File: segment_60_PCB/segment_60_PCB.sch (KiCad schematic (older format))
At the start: 118 parts, among them J1 BREAKOUT, SW1 SW_Push_45deg, SW10 SW_Push_45deg, SW11 SW_Push_45deg, SW12 SW_Push_45deg, SW13 SW_Push_45deg, SW14 SW_Push_45deg, SW15 SW_Push_45deg, SW16 SW_Push_45deg, SW17 SW_Push_45deg, SW18 SW_Push_45deg, SW19 SW_Push_45deg, SW2 SW_Push_45deg, SW20 SW_Push_45deg, SW21 SW_Push_45deg, SW22 SW_Push_45deg, SW23 SW_Push_45deg, SW24 SW_Push_45deg, SW25 SW_Push_45deg, SW26 SW_Push_45deg, SW27 SW_Push_45deg, SW28 SW_Push_45deg, SW29 SW_Push_45deg, SW3 SW_Push_45deg, SW30 SW_Push_45deg, SW31 SW_Push_45deg, SW32 SW_Push_45deg, SW33 SW_Push_45deg, SW34 SW_Push_45deg, SW35 SW_Push_45deg, SW36 SW_Push_45deg, SW37 SW_Push_45deg, SW38 SW_Push_45deg, SW39 SW_Push_45deg, SW4 SW_Push_45deg, SW40 SW_Push_45deg, SW41 SW_Push_45deg, SW42 SW_Push_45deg, SW43 SW_Push_45deg, SW44 SW_Push_45deg, SW45 SW_Push_45deg, SW46 SW_Push_45deg, SW47 SW_Push_45deg, SW48 SW_Push_45deg, SW49 SW_Push_45deg, SW5 SW_Push_45deg, SW50 SW_Push_45deg, SW51 SW_Push_45deg, SW52 SW_Push_45deg, SW53 SW_Push_45deg, SW54 SW_Push_45deg, SW55 SW_Push_45deg, SW56 SW_Push_45deg, SW57 SW_Push_45deg, SW58 SW_Push_45deg, SW59 SW_Push_45deg, SW6 SW_Push_45deg, SW60 SW_Push_45deg, SW61 SW_Push_45deg, SW62 SW_Push_45deg, SW63 SW_Push_45deg, SW64 SW_Push_45deg, SW65 SW_Push_45deg, SW66 SW_Push, SW67 SW_Push, SW7 SW_Push_45deg, SW8 SW_Push_45deg, SW9 SW_Push_45deg, U1 ATmega328P-PU, U10 74HC365, U11 74HC365, U12 74HC365, U13 74HC365, U14 74HC365, U15 74HC365, U16 74HC365, U17 74HC365, U2 74HC138, U3 74HC138, U4 74HC365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

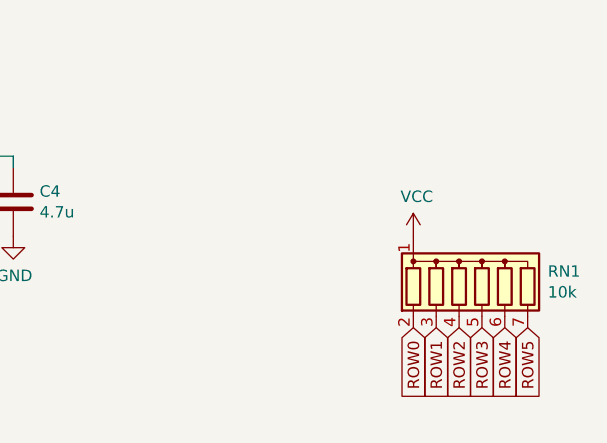
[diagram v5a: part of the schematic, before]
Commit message: added border, changed J1 footprint and model
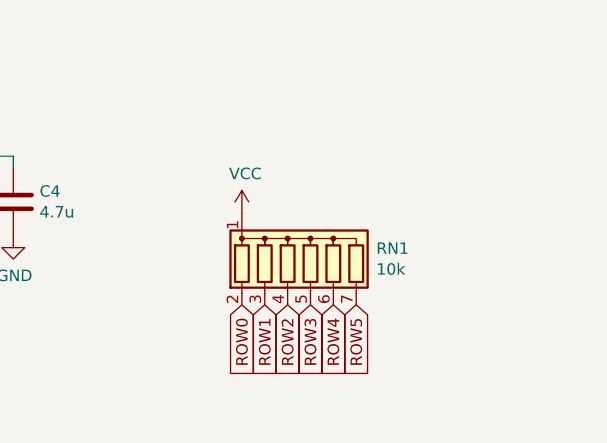
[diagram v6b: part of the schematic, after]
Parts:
- J1: footprint Connector_PinHeader_2.54mm:PinHeader_2x06_P2.54mm_Vertical -> Connector_IDC:IDC-Header_2x06_P2.54mm_Vertical
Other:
- moved on the sheet: RN1
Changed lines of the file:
@@
 L power:VCC #PWR0102
 U 1 1 62B23A0D
-P 15200 8650
-F 0 "#PWR0102" H 15200 8500 50  0001 C CNN
-F 1 "VCC" H 15215 8823 50  0000 C CNN
-F 2 "" H 15200 8650 50  0001 C CNN
-F 3 "" H 15200 8650 50  0001 C CNN
-	1    15200 8650
+P 14450 8550
+F 0 "#PWR0102" H 14450 8400 50  0001 C CNN
+F 1 "VCC" H 14465 8723 50  0000 C CNN
+F 2 "" H 14450 8550 50  0001 C CNN
+F 3 "" H 14450 8550 50  0001 C CNN
+	1    14450 8550
 	1    0    0    -1
 $EndComp
-Text GLabel 15700 9050 3    50   Input ~ 0
+Text GLabel 14950 8950 3    50   Input ~ 0
 ROW5
-Text GLabel 15600 9050 3    50   Input ~ 0
+Text GLabel 14850 8950 3    50   Input ~ 0
 ROW4
-Text GLabel 15500 9050 3    50   Input ~ 0
+Text GLabel 14750 8950 3    50   Input ~ 0
 ROW3
-Text GLabel 15400 9050 3    50   Input ~ 0
+Text GLabel 14650 8950 3    50   Input ~ 0
 ROW2
-Text GLabel 15300 9050 3    50   Input ~ 0
+Text GLabel 14550 8950 3    50   Input ~ 0
 ROW1
-Text GLabel 15200 9050 3    50   Input ~ 0
+Text GLabel 14450 8950 3    50   Input ~ 0
 ROW0
 $Comp
 L Device:R_Network06 RN1
 U 1 1 628AE35E
-P 15500 8850
-F 0 "RN1" H 15788 8896 50  0000 L CNN
-F 1 "10k" H 15788 8805 50  0000 L CNN
-F 2 "Resistor_THT:R_Array_SIP7" V 15875 8850 50  0001 C CNN
-F 3 "http://www.vishay.com/docs/31509/csc.pdf" H 15500 8850 50  0001 C CNN
-	1    15500 8850
+P 14750 8750
+F 0 "RN1" H 15038 8796 50  0000 L CNN
+F 1 "10k" H 15038 8705 50  0000 L CNN
+F 2 "Resistor_THT:R_Array_SIP7" V 15125 8750 50  0001 C CNN
+F 3 "http://www.vishay.com/docs/31509/csc.pdf" H 14750 8750 50  0001 C CNN
+	1    14750 8750
 	1    0    0    -1
 $EndComp
@@
 F 0 "J1" H 12650 9317 50  0000 C CNN
 F 1 "BREAKOUT" H 12650 9226 50  0000 C CNN
-F 2 "Connector_PinHeader_2.54mm:PinHeader_2x06_P2.54mm_Vertical" H 12600 8900 50  0001 C CNN
+F 2 "Connector_IDC:IDC-Header_2x06_P2.54mm_Vertical" H 12600 8900 50  0001 C CNN
 F 3 "~" H 12600 8900 50  0001 C CNN
 	1    12600 8900

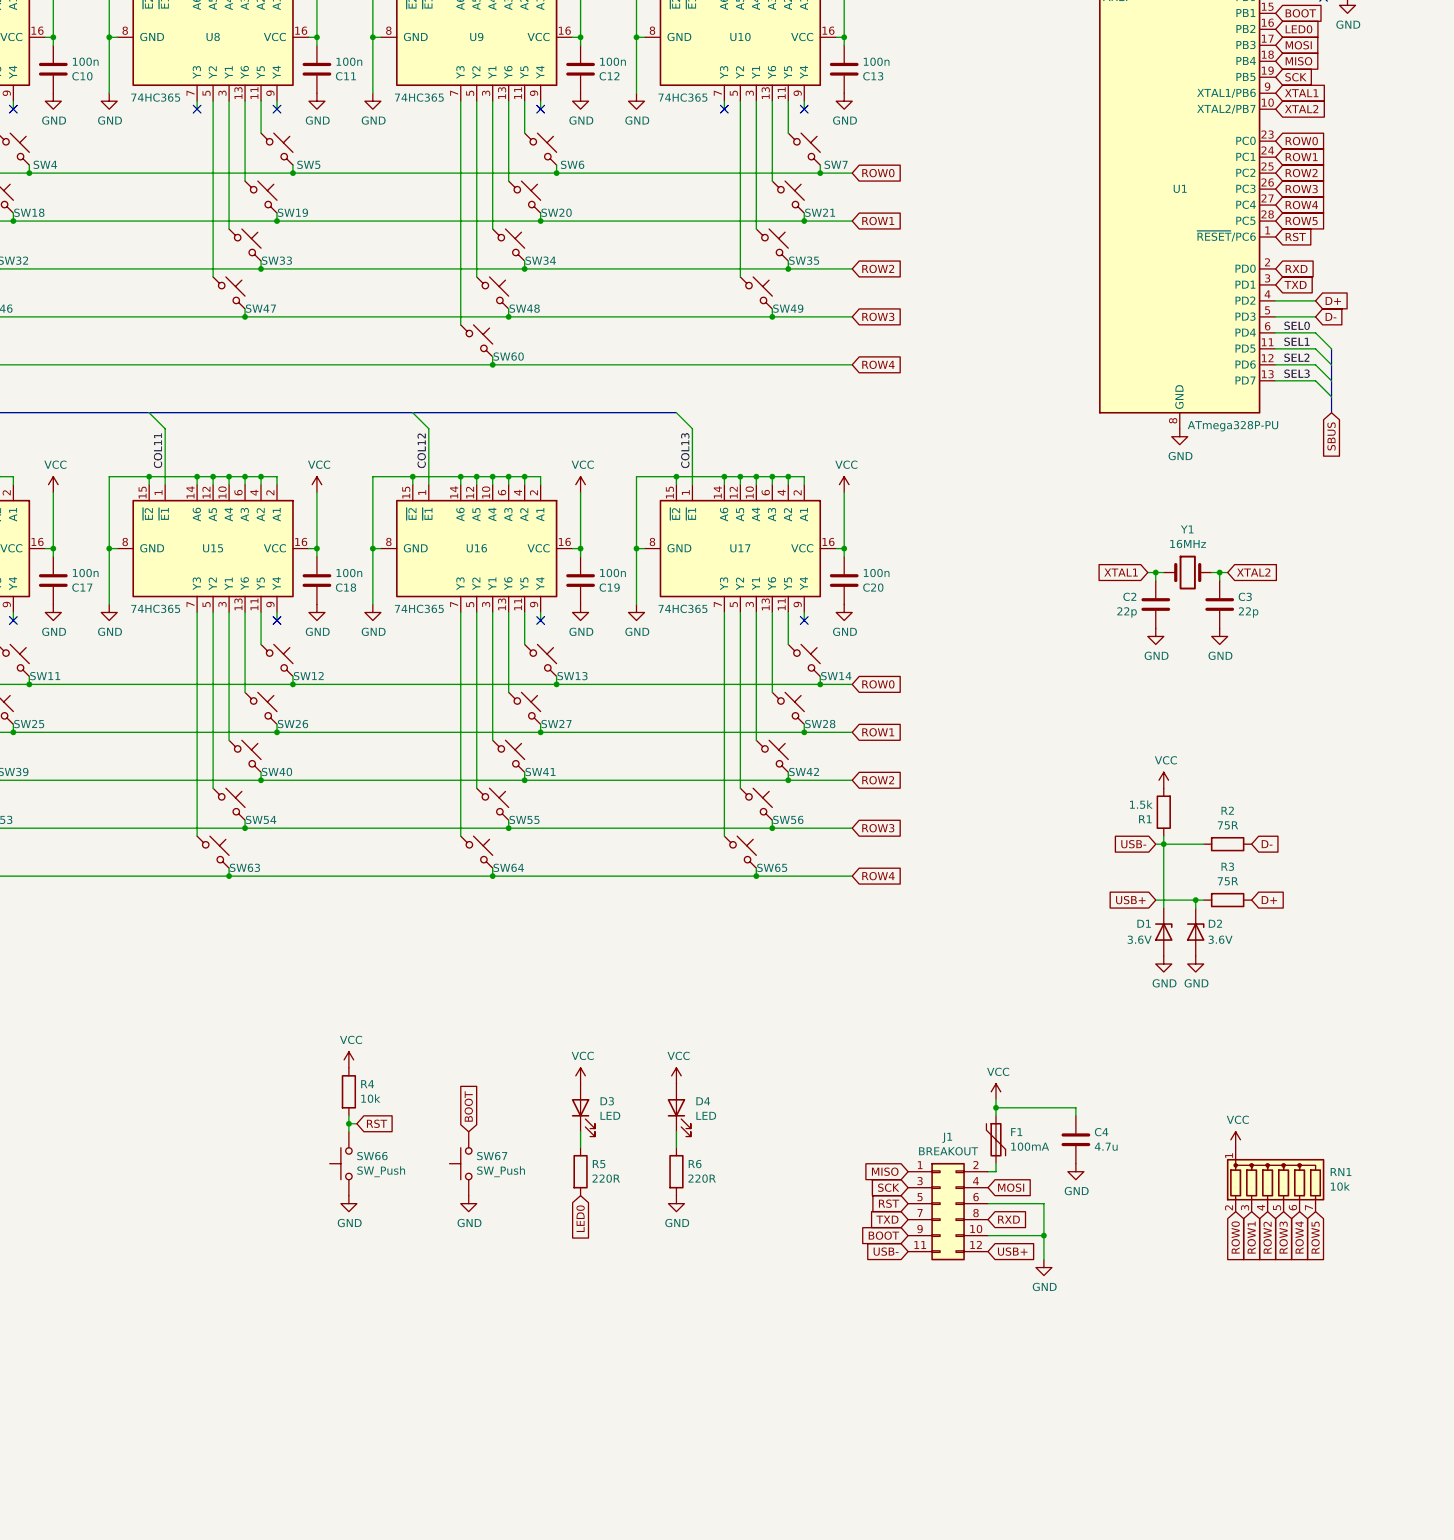
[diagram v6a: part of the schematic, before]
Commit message: Added power pours for VCC
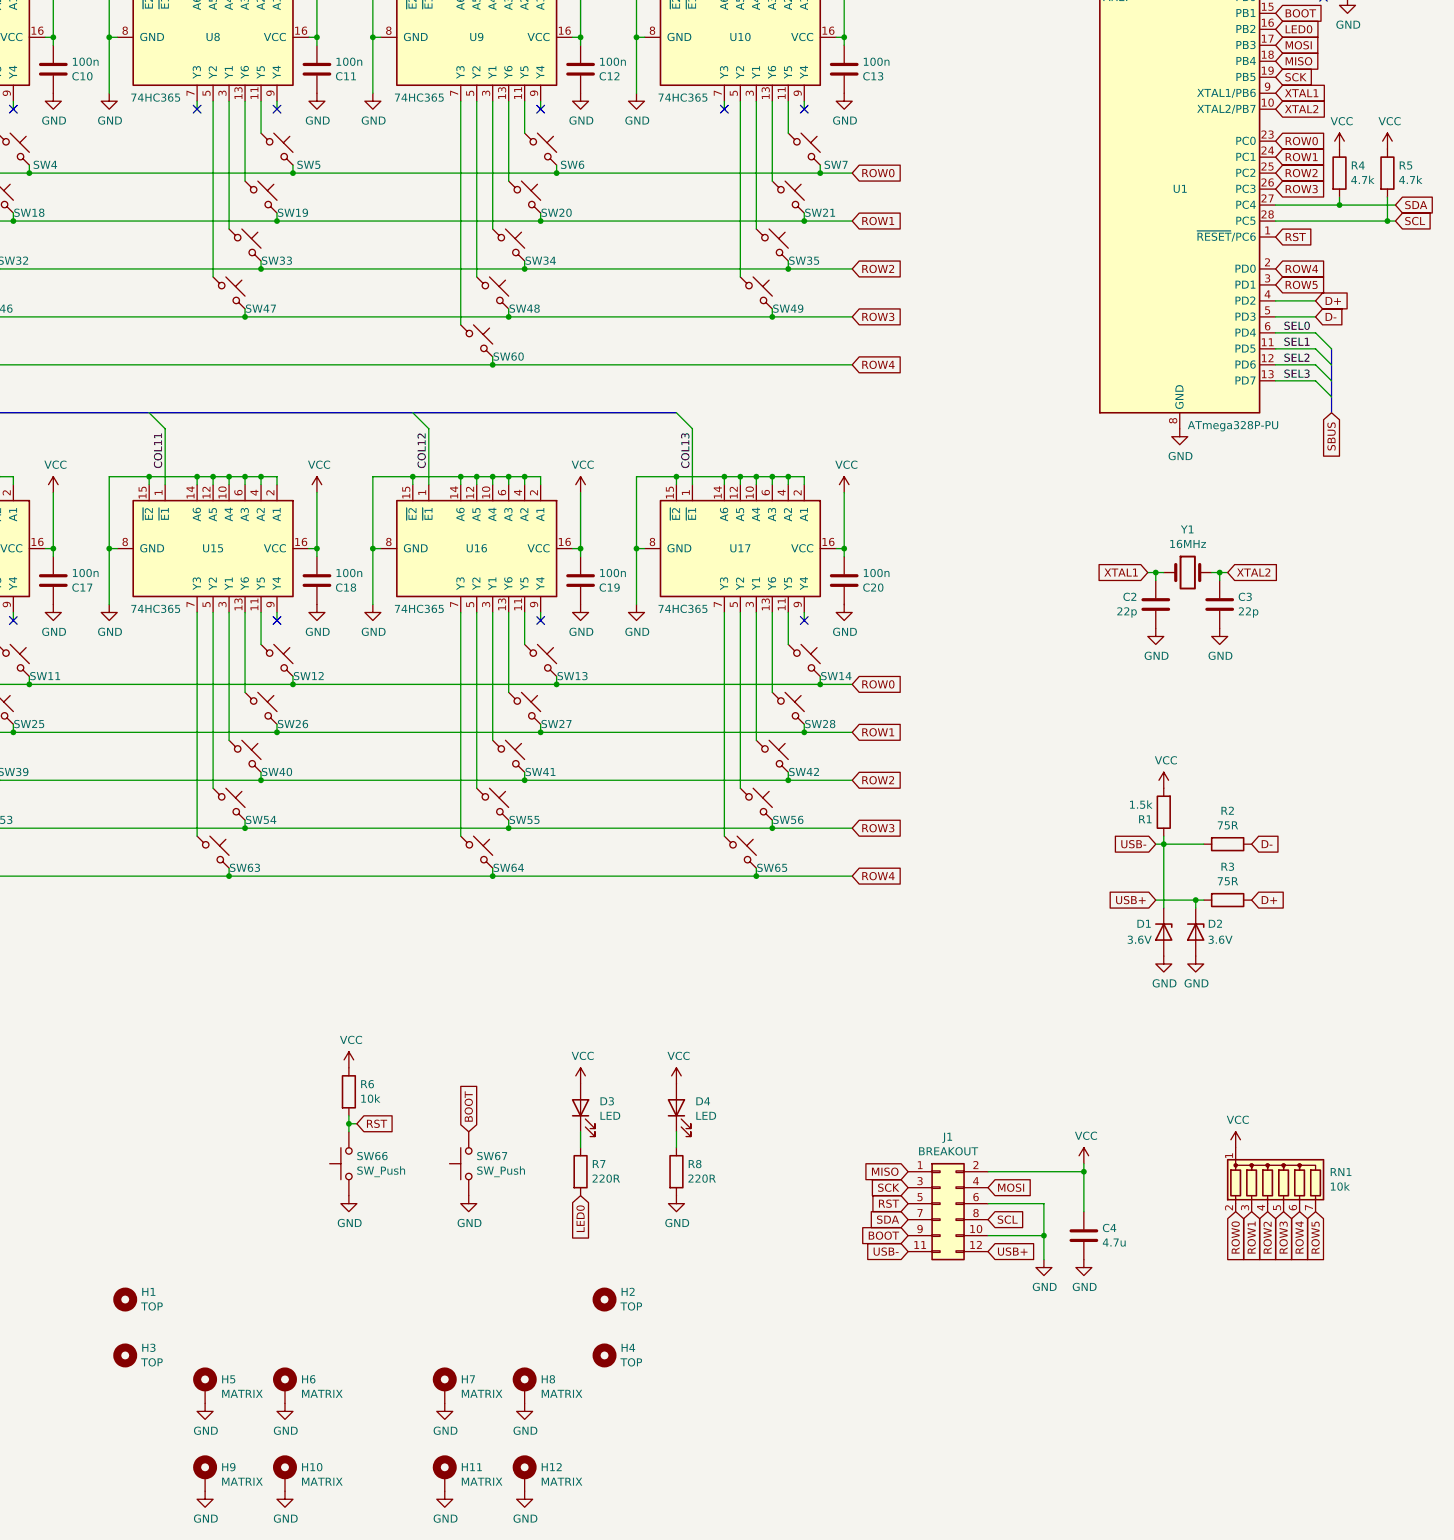
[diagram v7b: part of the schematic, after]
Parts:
- removed F1: 100mA, Fuse:Fuse_Littelfuse_395Series, symbol Device:Polyfuse
- added H1, H2, H3, H4: TOP, MountingHole:MountingHole_3.2mm_M3, symbol Mechanical:MountingHole
- added H10, H11, H12, H5, H6, H7, H8, H9: MATRIX, MountingHole:MountingHole_3.2mm_M3_Pad, symbol Mechanical:MountingHole_Pad
- added R4, R5: 4.7k, Resistor_THT:R_Axial_DIN0207_L6.3mm_D2.5mm_P10.16mm_Horizontal, symbol Device:R
- C1: footprint Capacitor_THT:C_Axial_L3.8mm_D2.6mm_P10.00mm_Horizontal -> Segment_Footprints:C_Axial_L3.8mm_D2.6mm_P10.16mm_Horizontal
- C10, C11, C12, C13, C14, C15, C16, C17, C18, C19, C20, C5, C6, C7, C8, C9: footprint Capacitor_THT:C_Axial_L3.8mm_D2.6mm_P7.50mm_Horizontal -> Segment_Footprints:C_Axial_L3.8mm_D2.6mm_P7.62mm_Horizontal
- renumbered R4 to R6, R5 to R7, R6 to R8
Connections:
- net GND: now also H10.1, H11.1, H12.1, H5.1, H6.1, H7.1, H8.1, H9.1
- net ROW4: now also U1.2 (PD0); no longer U1.27 (PC4)
- net ROW5: now also U1.3 (PD1); no longer U1.28 (PC5)
- net VCC: now also J1.2 (Pin_2), R4.1, R5.1
- net RXD renamed SCL
- net SCL: now also U1.28 (PC5), R5.2; no longer U1.2 (PD0)
- net TXD renamed SDA
- net SDA: now also U1.27 (PC4), R4.2; no longer U1.3 (PD1)
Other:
- moved on the sheet: C4
